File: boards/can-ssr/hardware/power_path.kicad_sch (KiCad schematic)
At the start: 24 parts, among them Q1 IPB110N20N3LF, Q2 IPB110N20N3LF, Q3 IPB110N20N3LF, Q4 IPB110N20N3LF, Q5 MMBT2907A, U10 VOM1271T, U11 VOM1271T, U12 ACS770ECB-100U-PFF-T

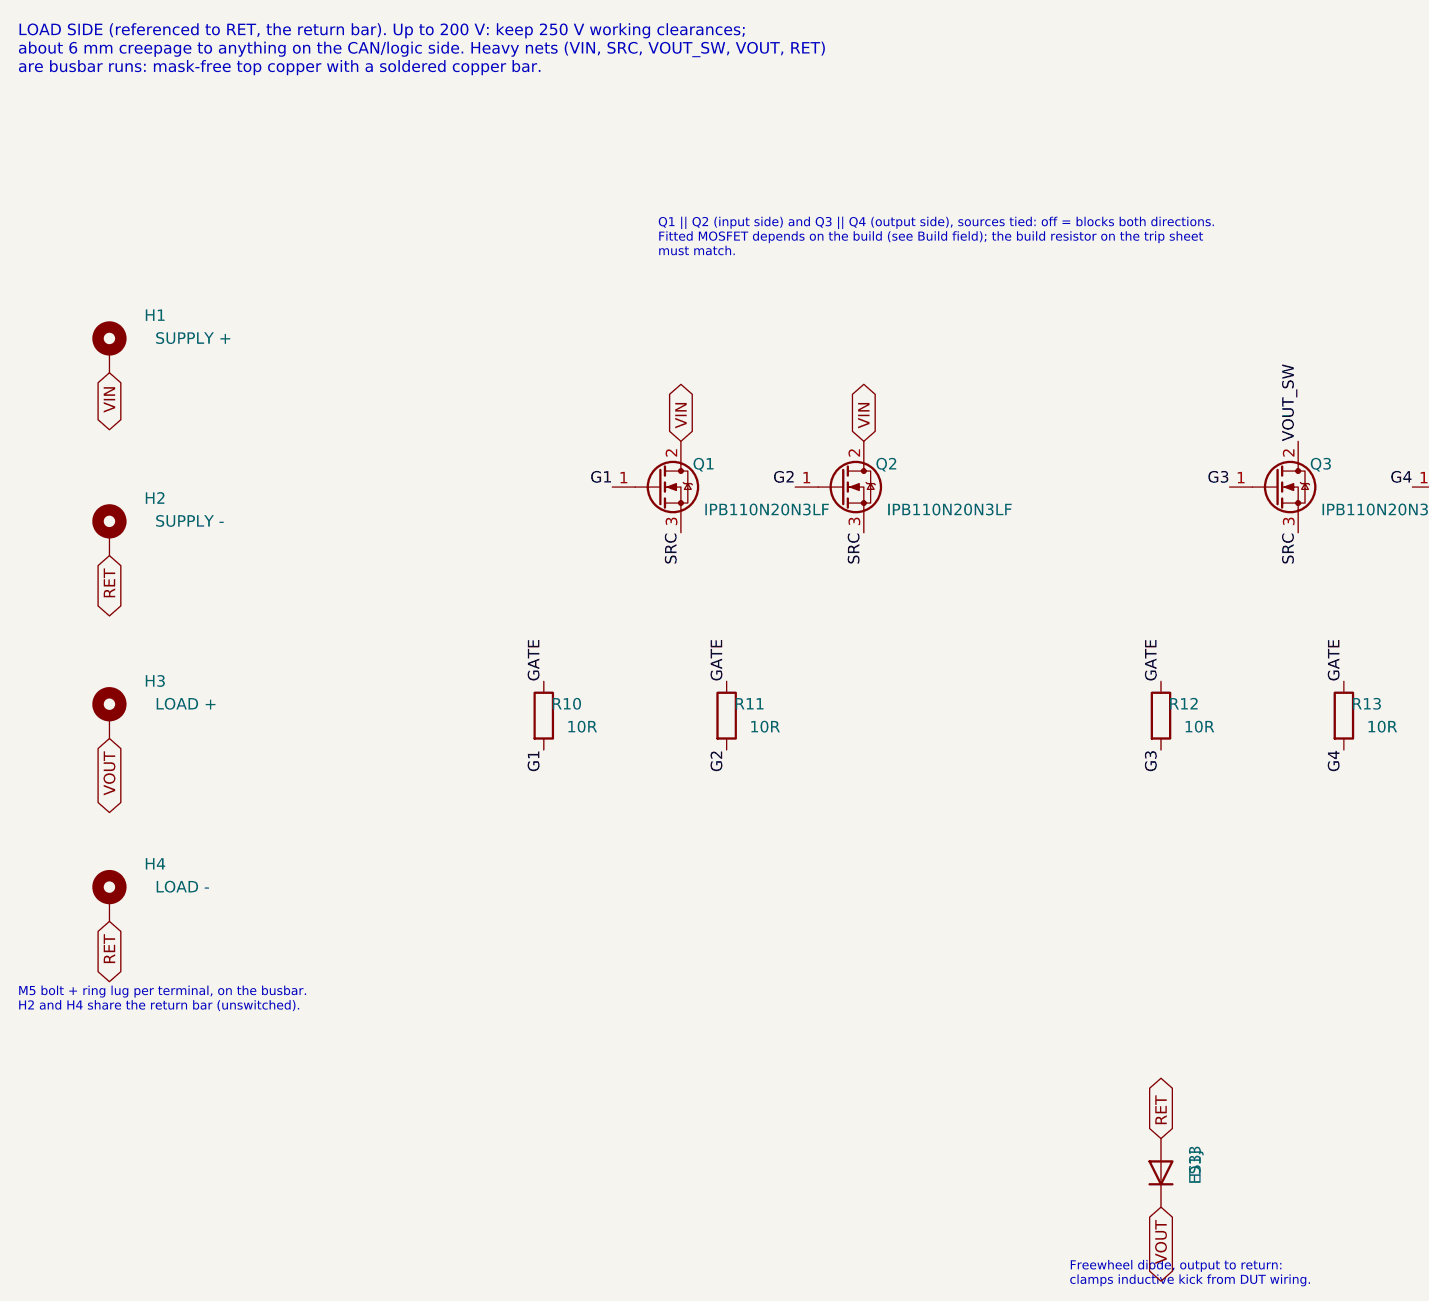
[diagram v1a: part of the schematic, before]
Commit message: can-ssr schematic: load-side sense and Mean Well control block
- UCC12050 isolated 5 V (reinforced) and ISO1640DWR I2C isolator (wide
  body, reinforced) are the only crossings into the load domain
- MCP3428 ADC: Vin and Vout through 3 x 332k / 8.06k dividers (250 V FS,
  ~200 Hz anti-aliasing), plus PV/PC readback at the terminal
- Two MCP4725 DACs (0x60, 0x61) drive the Mean Well PV and PC inputs via
  1k; TLP222A photorelay closes Remote ON/OFF, off at reset
- J30: 5-pole Phoenix MC 3.5 mm for the Mean Well control wires
- Load-side ground net renamed GND_LOAD (the RET return bar) so ERC
  recognises it as a ground
- New symbols Thl_Isolator:ISO1640DWR and UCC12050DVE from the TI
  datasheets; stock imports for MCP3428, MCP4725, TLP222A, SOIC-16W/14,
  SOT-23-6, DIP-4, 5-pole MC header

Co-Authored-By: Claude Opus 5.5 <noreply@anthropic.com>
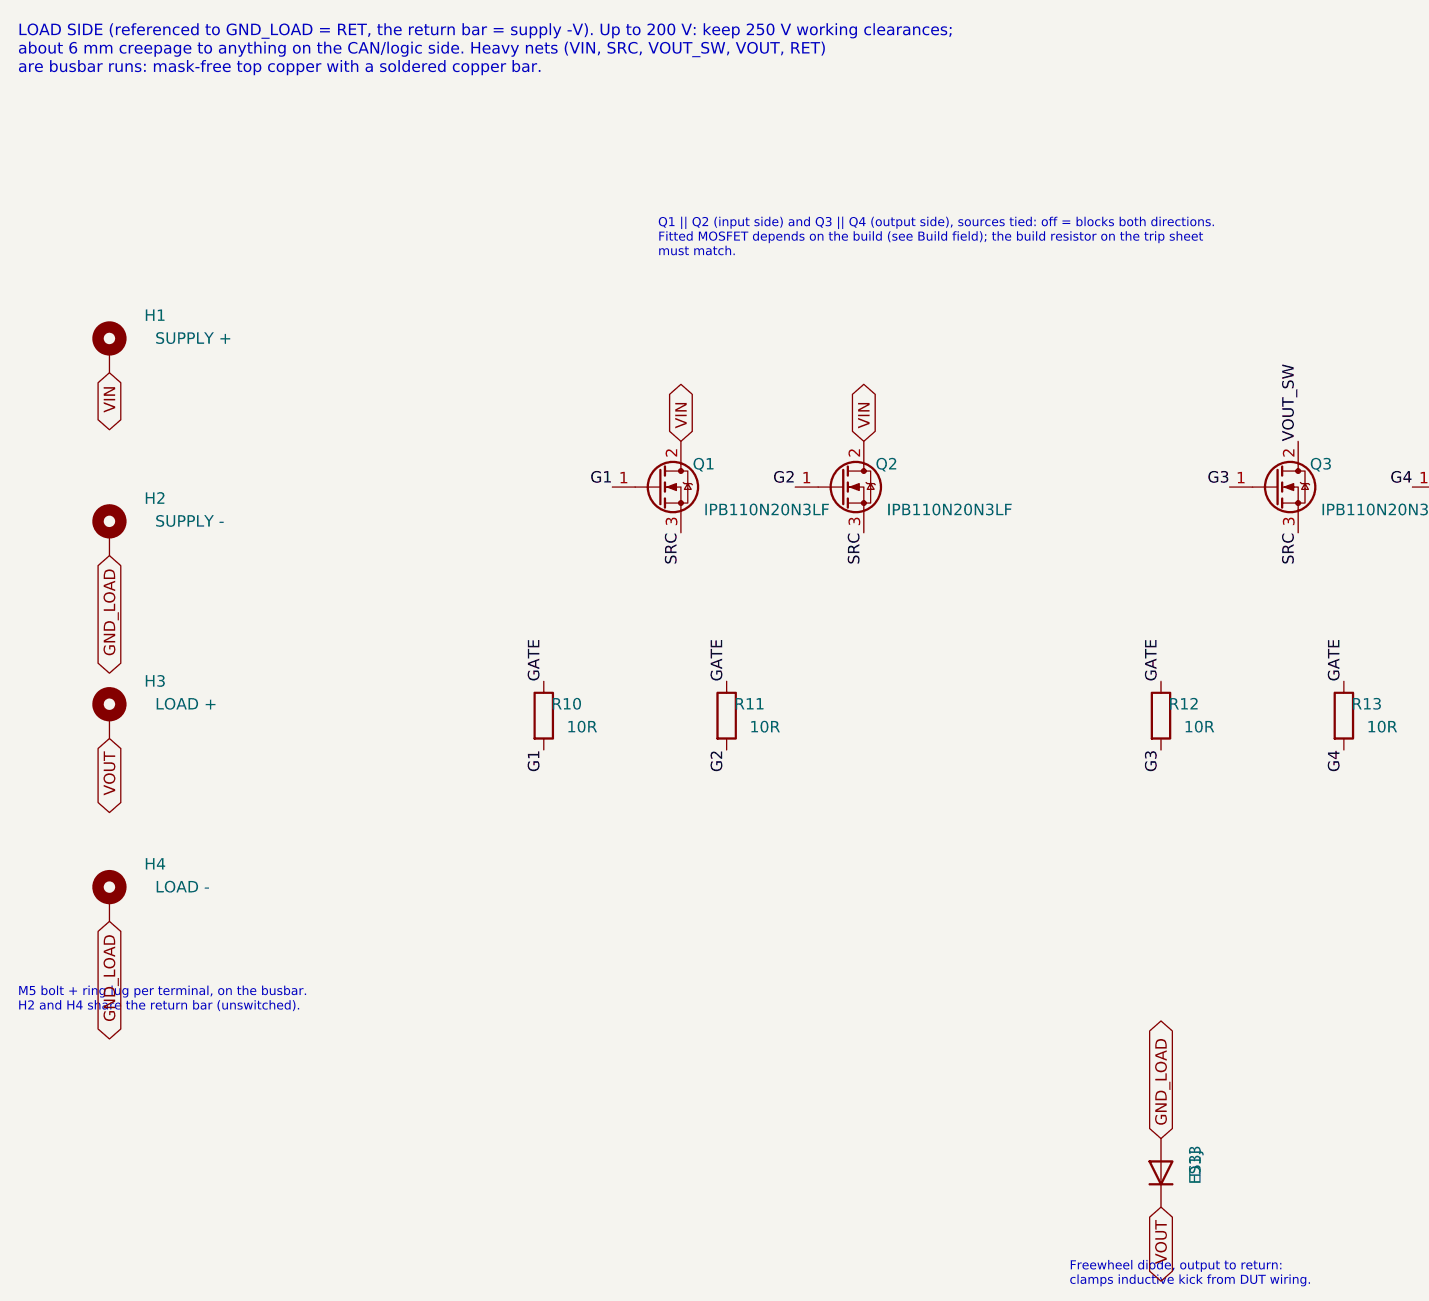
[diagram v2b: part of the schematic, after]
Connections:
- net RET renamed GND_LOAD
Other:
- note added: "LOAD SIDE (referenced to GND_LOAD = RET, the return bar = supply -V). Up to 200 V: keep 250 V working clearances; about 6 mm creepage to anything on the CAN/logic side. Heavy nets (VIN, SRC, VOUT_SW, VOUT, RET) are busbar runs: mask-free top copper with a soldered copper bar."
- note removed: "LOAD SIDE (referenced to RET, the return bar). Up to 200 V: keep 250 V working clearances; about 6 mm creepage to anything on the CAN/logic side. Heavy nets (VIN, SRC, VOUT_SW, VOUT, RET) are busbar runs: mask-free top copper with a soldered copper bar."
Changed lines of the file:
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@@
 		(rev "A")
 	)
-	(text "LOAD SIDE (referenced to RET, the return bar). Up to 200 V: keep 250 V working clearances;\nabout 6 mm creepage to anything on the CAN/logic side. Heavy nets (VIN, SRC, VOUT_SW, VOUT, RET)\nare busbar runs: mask-free top copper with a soldered copper bar."
+	(text "LOAD SIDE (referenced to GND_LOAD = RET, the return bar = supply -V). Up to 200 V: keep 250 V working clearances;\nabout 6 mm creepage to anything on the CAN/logic side. Heavy nets (VIN, SRC, VOUT_SW, VOUT, RET)\nare busbar runs: mask-free top copper with a soldered copper bar."
 		(exclude_from_sim no)
 		(at 25.4 30.48 0)
@@
 		(instances
 			(project "can-ssr"
-				(path "/09b96810-cbdb-496a-83a0-e49ecf8d36fe/c64a2bd9-5497-4e3f-a10e-ded04b8c077f"
+				(path "/09b96810-cbdb-496a-83a0-e49ecf8d36fe/064504af-df1e-403e-8d8a-7ae59a780357"
 					(reference "H1")
 					(unit 1)
@@
 		(instances
 			(project "can-ssr"
-				(path "/09b96810-cbdb-496a-83a0-e49ecf8d36fe/c64a2bd9-5497-4e3f-a10e-ded04b8c077f"
+				(path "/09b96810-cbdb-496a-83a0-e49ecf8d36fe/064504af-df1e-403e-8d8a-7ae59a780357"
 					(reference "H2")
 					(unit 1)
@@
 		)
 	)
-	(global_label "RET"
+	(global_label "GND_LOAD"
 		(shape bidirectional)
 		(at 35.56 83.82 270)
@@
 		(instances
 			(project "can-ssr"
-				(path "/09b96810-cbdb-496a-83a0-e49ecf8d36fe/c64a2bd9-5497-4e3f-a10e-ded04b8c077f"
+				(path "/09b96810-cbdb-496a-83a0-e49ecf8d36fe/064504af-df1e-403e-8d8a-7ae59a780357"
 					(reference "H3")
 					(unit 1)
@@
 		(instances
 			(project "can-ssr"
-				(path "/09b96810-cbdb-496a-83a0-e49ecf8d36fe/c64a2bd9-5497-4e3f-a10e-ded04b8c077f"
+				(path "/09b96810-cbdb-496a-83a0-e49ecf8d36fe/064504af-df1e-403e-8d8a-7ae59a780357"
 					(reference "H4")
 					(unit 1)
@@
 		)
 	)
-	(global_label "RET"
+	(global_label "GND_LOAD"
 		(shape bidirectional)
 		(at 35.56 124.46 270)
@@
 		(instances
 			(project "can-ssr"
-				(path "/09b96810-cbdb-496a-83a0-e49ecf8d36fe/c64a2bd9-5497-4e3f-a10e-ded04b8c077f"
+				(path "/09b96810-cbdb-496a-83a0-e49ecf8d36fe/064504af-df1e-403e-8d8a-7ae59a780357"
 					(reference "Q1")
 					(unit 1)
@@
 		(instances
 			(project "can-ssr"
-				(path "/09b96810-cbdb-496a-83a0-e49ecf8d36fe/c64a2bd9-5497-4e3f-a10e-ded04b8c077f"
+				(path "/09b96810-cbdb-496a-83a0-e49ecf8d36fe/064504af-df1e-403e-8d8a-7ae59a780357"
 					(reference "Q2")
 					(unit 1)
@@
 		(instances
 			(project "can-ssr"
-				(path "/09b96810-cbdb-496a-83a0-e49ecf8d36fe/c64a2bd9-5497-4e3f-a10e-ded04b8c077f"
+				(path "/09b96810-cbdb-496a-83a0-e49ecf8d36fe/064504af-df1e-403e-8d8a-7ae59a780357"
 					(reference "Q3")
 					(unit 1)
@@
 		(instances
 			(project "can-ssr"
-				(path "/09b96810-cbdb-496a-83a0-e49ecf8d36fe/c64a2bd9-5497-4e3f-a10e-ded04b8c077f"
+				(path "/09b96810-cbdb-496a-83a0-e49ecf8d36fe/064504af-df1e-403e-8d8a-7ae59a780357"
 					(reference "Q4")
 					(unit 1)
@@
 		(instances
 			(project "can-ssr"
-				(path "/09b96810-cbdb-496a-83a0-e49ecf8d36fe/c64a2bd9-5497-4e3f-a10e-ded04b8c077f"
+				(path "/09b96810-cbdb-496a-83a0-e49ecf8d36fe/064504af-df1e-403e-8d8a-7ae59a780357"
 					(reference "R10")
 					(unit 1)
@@
 		(instances
 			(project "can-ssr"
-				(path "/09b96810-cbdb-496a-83a0-e49ecf8d36fe/c64a2bd9-5497-4e3f-a10e-ded04b8c077f"
+				(path "/09b96810-cbdb-496a-83a0-e49ecf8d36fe/064504af-df1e-403e-8d8a-7ae59a780357"
 					(reference "R11")
 					(unit 1)
@@
 		(instances
 			(project "can-ssr"
-				(path "/09b96810-cbdb-496a-83a0-e49ecf8d36fe/c64a2bd9-5497-4e3f-a10e-ded04b8c077f"
+				(path "/09b96810-cbdb-496a-83a0-e49ecf8d36fe/064504af-df1e-403e-8d8a-7ae59a780357"
 					(reference "R12")
 					(unit 1)
@@
 		(instances
 			(project "can-ssr"
-				(path "/09b96810-cbdb-496a-83a0-e49ecf8d36fe/c64a2bd9-5497-4e3f-a10e-ded04b8c077f"
+				(path "/09b96810-cbdb-496a-83a0-e49ecf8d36fe/064504af-df1e-403e-8d8a-7ae59a780357"
 					(reference "R13")
 					(unit 1)
@@
 		(instances
 			(project "can-ssr"
-				(path "/09b96810-cbdb-496a-83a0-e49ecf8d36fe/c64a2bd9-5497-4e3f-a10e-ded04b8c077f"
+				(path "/09b96810-cbdb-496a-83a0-e49ecf8d36fe/064504af-df1e-403e-8d8a-7ae59a780357"
 					(reference "R14")
 					(unit 1)
@@
 		(instances
 			(project "can-ssr"
-				(path "/09b96810-cbdb-496a-83a0-e49ecf8d36fe/c64a2bd9-5497-4e3f-a10e-ded04b8c077f"
+				(path "/09b96810-cbdb-496a-83a0-e49ecf8d36fe/064504af-df1e-403e-8d8a-7ae59a780357"
 					(reference "D10")
 					(unit 1)
@@
 		(instances
 			(project "can-ssr"
-				(path "/09b96810-cbdb-496a-83a0-e49ecf8d36fe/c64a2bd9-5497-4e3f-a10e-ded04b8c077f"
+				(path "/09b96810-cbdb-496a-83a0-e49ecf8d36fe/064504af-df1e-403e-8d8a-7ae59a780357"
 					(reference "D11")
 					(unit 1)
@@
 		(instances
 			(project "can-ssr"
-				(path "/09b96810-cbdb-496a-83a0-e49ecf8d36fe/c64a2bd9-5497-4e3f-a10e-ded04b8c077f"
+				(path "/09b96810-cbdb-496a-83a0-e49ecf8d36fe/064504af-df1e-403e-8d8a-7ae59a780357"
 					(reference "Q5")
 					(unit 1)
@@
 		(instances
 			(project "can-ssr"
-				(path "/09b96810-cbdb-496a-83a0-e49ecf8d36fe/c64a2bd9-5497-4e3f-a10e-ded04b8c077f"
+				(path "/09b96810-cbdb-496a-83a0-e49ecf8d36fe/064504af-df1e-403e-8d8a-7ae59a780357"
 					(reference "C10")
 					(unit 1)
@@
 		(instances
 			(project "can-ssr"
-				(path "/09b96810-cbdb-496a-83a0-e49ecf8d36fe/c64a2bd9-5497-4e3f-a10e-ded04b8c077f"
+				(path "/09b96810-cbdb-496a-83a0-e49ecf8d36fe/064504af-df1e-403e-8d8a-7ae59a780357"
 					(reference "D12")
 					(unit 1)
@@
 		(instances
 			(project "can-ssr"
-				(path "/09b96810-cbdb-496a-83a0-e49ecf8d36fe/c64a2bd9-5497-4e3f-a10e-ded04b8c077f"
+				(path "/09b96810-cbdb-496a-83a0-e49ecf8d36fe/064504af-df1e-403e-8d8a-7ae59a780357"
 					(reference "R15")
 					(unit 1)
@@
 		(instances
 			(project "can-ssr"
-				(path "/09b96810-cbdb-496a-83a0-e49ecf8d36fe/c64a2bd9-5497-4e3f-a10e-ded04b8c077f"
+				(path "/09b96810-cbdb-496a-83a0-e49ecf8d36fe/064504af-df1e-403e-8d8a-7ae59a780357"
 					(reference "U10")
 					(unit 1)
@@
 		(instances
 			(project "can-ssr"
-				(path "/09b96810-cbdb-496a-83a0-e49ecf8d36fe/c64a2bd9-5497-4e3f-a10e-ded04b8c077f"
+				(path "/09b96810-cbdb-496a-83a0-e49ecf8d36fe/064504af-df1e-403e-8d8a-7ae59a780357"
 					(reference "U11")
 					(unit 1)
@@
 		(instances
 			(project "can-ssr"
-				(path "/09b96810-cbdb-496a-83a0-e49ecf8d36fe/c64a2bd9-5497-4e3f-a10e-ded04b8c077f"
+				(path "/09b96810-cbdb-496a-83a0-e49ecf8d36fe/064504af-df1e-403e-8d8a-7ae59a780357"
 					(reference "U12")
 					(unit 1)
@@
 		(instances
 			(project "can-ssr"
-				(path "/09b96810-cbdb-496a-83a0-e49ecf8d36fe/c64a2bd9-5497-4e3f-a10e-ded04b8c077f"
+				(path "/09b96810-cbdb-496a-83a0-e49ecf8d36fe/064504af-df1e-403e-8d8a-7ae59a780357"
 					(reference "#PWR01")
 					(unit 1)
@@
 		(instances
 			(project "can-ssr"
-				(path "/09b96810-cbdb-496a-83a0-e49ecf8d36fe/c64a2bd9-5497-4e3f-a10e-ded04b8c077f"
+				(path "/09b96810-cbdb-496a-83a0-e49ecf8d36fe/064504af-df1e-403e-8d8a-7ae59a780357"
 					(reference "#PWR02")
 					(unit 1)
@@
 		(instances
 			(project "can-ssr"
-				(path "/09b96810-cbdb-496a-83a0-e49ecf8d36fe/c64a2bd9-5497-4e3f-a10e-ded04b8c077f"
+				(path "/09b96810-cbdb-496a-83a0-e49ecf8d36fe/064504af-df1e-403e-8d8a-7ae59a780357"
 					(reference "C11")
 					(unit 1)
@@
 		(instances
 			(project "can-ssr"
-				(path "/09b96810-cbdb-496a-83a0-e49ecf8d36fe/c64a2bd9-5497-4e3f-a10e-ded04b8c077f"
+				(path "/09b96810-cbdb-496a-83a0-e49ecf8d36fe/064504af-df1e-403e-8d8a-7ae59a780357"
 					(reference "#PWR03")
 					(unit 1)
@@
 		(instances
 			(project "can-ssr"
-				(path "/09b96810-cbdb-496a-83a0-e49ecf8d36fe/c64a2bd9-5497-4e3f-a10e-ded04b8c077f"
+				(path "/09b96810-cbdb-496a-83a0-e49ecf8d36fe/064504af-df1e-403e-8d8a-7ae59a780357"
 					(reference "#PWR04")
 					(unit 1)
@@
 		(instances
 			(project "can-ssr"
-				(path "/09b96810-cbdb-496a-83a0-e49ecf8d36fe/c64a2bd9-5497-4e3f-a10e-ded04b8c077f"
+				(path "/09b96810-cbdb-496a-83a0-e49ecf8d36fe/064504af-df1e-403e-8d8a-7ae59a780357"
 					(reference "D13")
 					(unit 1)
@@
 		)
 	)
-	(global_label "RET"
+	(global_label "GND_LOAD"
 		(shape bidirectional)
 		(at 152.4 148.59 90)
